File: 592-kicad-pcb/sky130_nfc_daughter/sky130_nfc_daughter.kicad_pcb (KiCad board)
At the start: 4 copper layers, 50 x 52 mm, 198 parts, among them J1 U.FL-R-SMT-1_80_, J10 U.FL-R-SMT-1_80_, J2 U.FL-R-SMT-1_80_, J3 U.FL-R-SMT-1_80_, J4 U.FL-R-SMT-1_80_, J5 U.FL-R-SMT-1_80_, J6 U.FL-R-SMT-1_80_, J7 U.FL-R-SMT-1_80_, J8 DF40C-40DS-0.4V_51_, J9 DF40C-40DS-0.4V_51_, SW1 SW_Push, U1 Caravel_QFN, U3 W25Q32JVZP

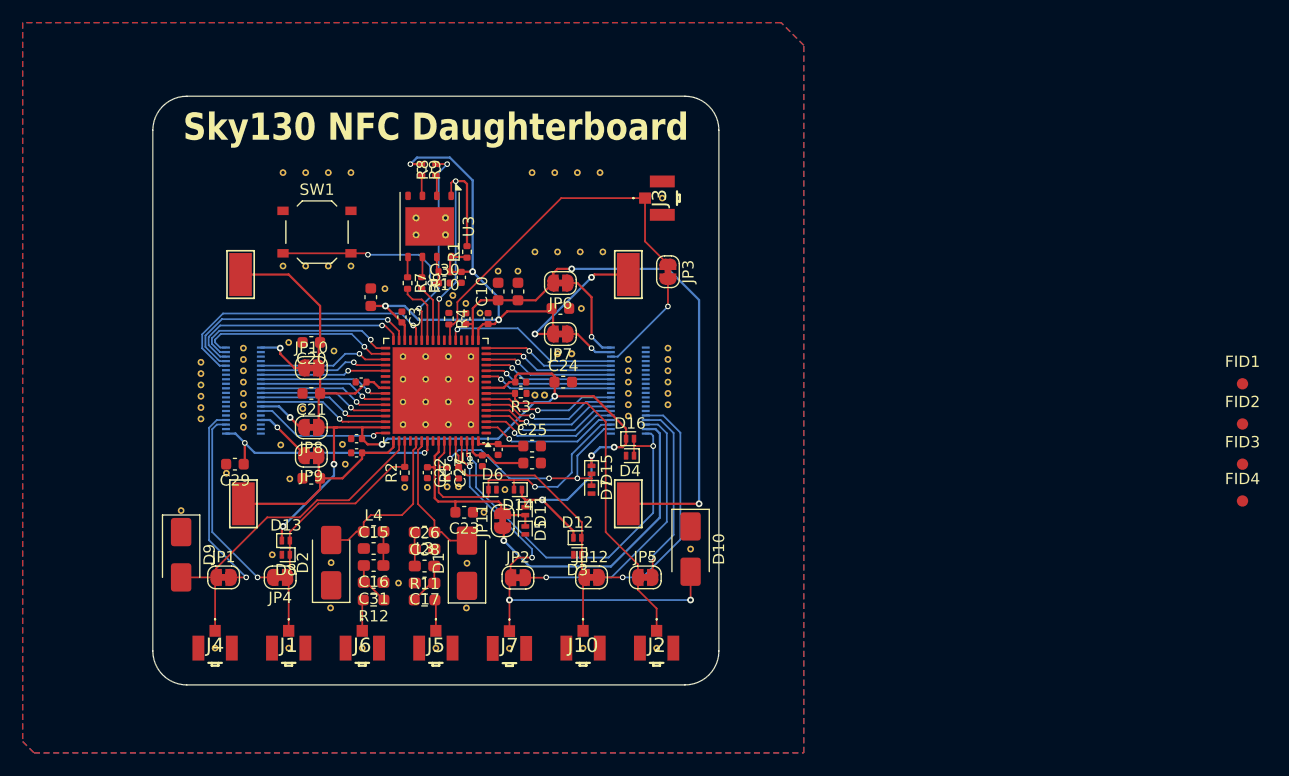
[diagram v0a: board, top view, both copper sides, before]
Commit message: finish daughter routing + silk
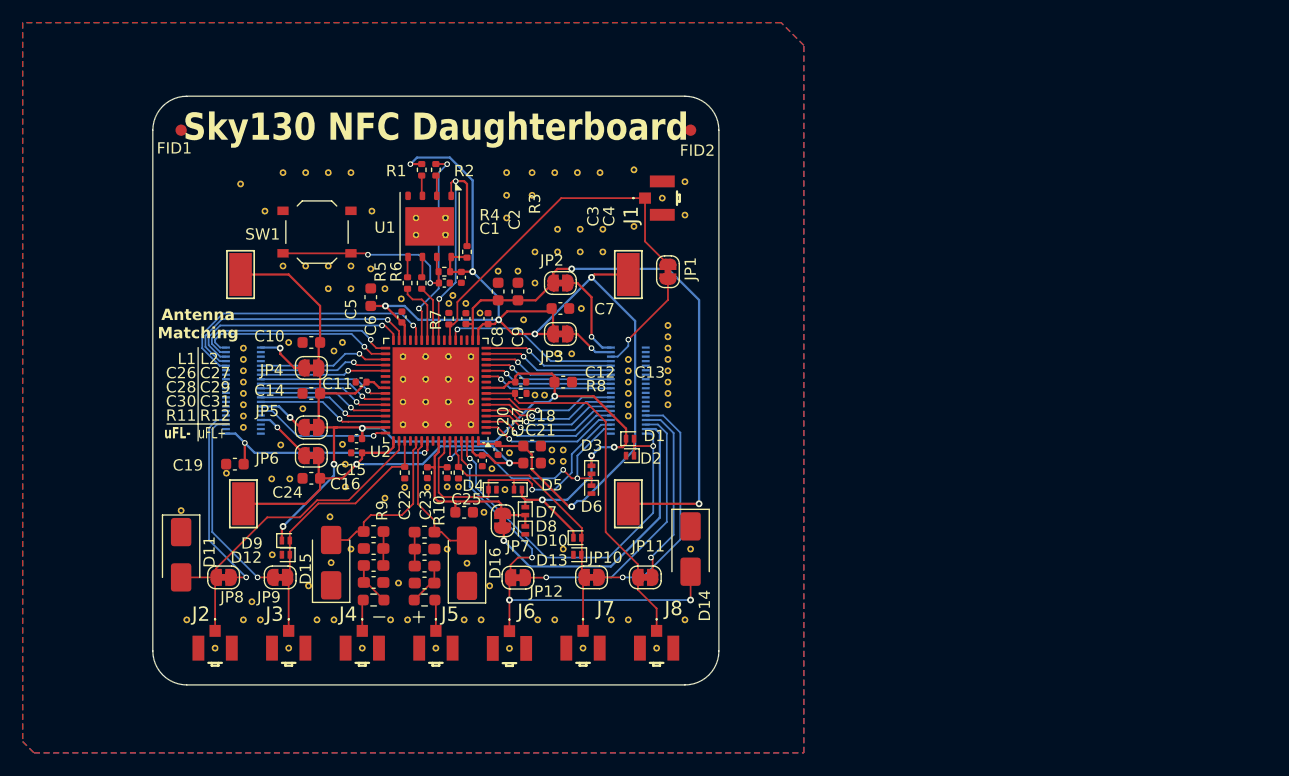
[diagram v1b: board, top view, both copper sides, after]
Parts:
- removed the ? at (53.8, 43.5)
- removed the ? at (53.8, 45.5)
- removed the ? at (53.8, 46.5)
- removed the ? at (53.8, 47.5)
- removed the ? at (53.8, 48.5)
- removed the ? at (53.8, 44.5)
- removed FID3, FID4: Fiducial, Fiducial:Fiducial_1mm_Mask2mm
- added ?: STITCHING_VIA_0p3mm, 592-partslib:STITCHING_VIA_0p3mm, F.Cu at (57.5, 66.2)
- added ?: STITCHING_VIA_0p3mm, 592-partslib:STITCHING_VIA_0p3mm, F.Cu at (70.5, 66.2)
- added ?: STITCHING_VIA_0p3mm, 592-partslib:STITCHING_VIA_0p3mm, F.Cu at (92.0, 31.5)
- added ?: STITCHING_VIA_0p3mm, 592-partslib:STITCHING_VIA_0p3mm, F.Cu at (78.5, 66.2)
- added ?: STITCHING_VIA_0p3mm, 592-partslib:STITCHING_VIA_0p3mm, F.Cu at (96.5, 30.5)
- added ?: STITCHING_VIA_0p3mm, 592-partslib:STITCHING_VIA_0p3mm, F.Cu at (85.8, 51.2)
- added ?: STITCHING_VIA_0p3mm, 592-partslib:STITCHING_VIA_0p3mm, F.Cu at (92.0, 26.5)
- added ?: STITCHING_VIA_0p3mm, 592-partslib:STITCHING_VIA_0p3mm, F.Cu at (85.0, 66.2)
- added ?: STITCHING_VIA_0p3mm, 592-partslib:STITCHING_VIA_0p3mm, F.Cu at (83.5, 66.2)
- added ?: STITCHING_VIA_0p3mm, 592-partslib:STITCHING_VIA_0p3mm, F.Cu at (52.5, 66.2)
- added ?: STITCHING_VIA_0p3mm, 592-partslib:STITCHING_VIA_0p3mm, F.Cu at (87.2, 31.8)
- added ?: STITCHING_VIA_0p3mm, 592-partslib:STITCHING_VIA_0p3mm, F.Cu at (96.5, 27.6)
- added ?: STITCHING_VIA_0p3mm, 592-partslib:STITCHING_VIA_0p3mm, F.Cu at (95.0, 41.2)
- added ?: STITCHING_VIA_0p3mm, 592-partslib:STITCHING_VIA_0p3mm, F.Cu at (59.4, 30.1)
- added ?: STITCHING_VIA_0p3mm, 592-partslib:STITCHING_VIA_0p3mm, F.Cu at (57.2, 27.8)
- added ?: STITCHING_VIA_0p3mm, 592-partslib:STITCHING_VIA_0p3mm, F.Cu at (58.2, 64.7)
- added ?: STITCHING_VIA_0p3mm, 592-partslib:STITCHING_VIA_0p3mm, F.Cu at (65.2, 57.1)
- added ?: STITCHING_VIA_0p3mm, 592-partslib:STITCHING_VIA_0p3mm, F.Cu at (96.5, 66.2)
- added ?: STITCHING_VIA_0p3mm, 592-partslib:STITCHING_VIA_0p3mm, F.Cu at (84.8, 51.2)
- added ?: STITCHING_VIA_0p3mm, 592-partslib:STITCHING_VIA_0p3mm, F.Cu at (80.8, 26.8)
- added ?: STITCHING_VIA_0p3mm, 592-partslib:STITCHING_VIA_0p3mm, F.Cu at (84.8, 52.2)
- added ?: STITCHING_VIA_0p3mm, 592-partslib:STITCHING_VIA_0p3mm, F.Cu at (91.5, 66.2)
- added ?: STITCHING_VIA_0p3mm, 592-partslib:STITCHING_VIA_0p3mm, F.Cu at (79.5, 52.9)
- added ?: STITCHING_VIA_0p3mm, 592-partslib:STITCHING_VIA_0p3mm, F.Cu at (65.5, 66.2)
- added ?: STITCHING_VIA_0p3mm, 592-partslib:STITCHING_VIA_0p3mm, F.Cu at (77.0, 66.2)
- added ?: STITCHING_VIA_0p3mm, 592-partslib:STITCHING_VIA_0p3mm, F.Cu at (72.0, 66.2)
- added ?: STITCHING_VIA_0p3mm, 592-partslib:STITCHING_VIA_0p3mm, F.Cu at (67.0, 60.0)
- added ?: STITCHING_VIA_0p3mm, 592-partslib:STITCHING_VIA_0p3mm, F.Cu at (82.2, 39.8)
- added ?: STITCHING_VIA_0p3mm, 592-partslib:STITCHING_VIA_0p3mm, F.Cu at (81.0, 51.5)
- added ?: STITCHING_VIA_0p3mm, 592-partslib:STITCHING_VIA_0p3mm, F.Cu at (83.0, 28.8)
- added ?: STITCHING_VIA_0p3mm, 592-partslib:STITCHING_VIA_0p3mm, F.Cu at (70.0, 55.5)
- added ?: STITCHING_VIA_0p3mm, 592-partslib:STITCHING_VIA_0p3mm, F.Cu at (83.2, 36.5)
- added ?: STITCHING_VIA_0p3mm, 592-partslib:STITCHING_VIA_0p3mm, F.Cu at (95.0, 40.2)
- added ?: STITCHING_VIA_0p3mm, 592-partslib:STITCHING_VIA_0p3mm, F.Cu at (65.0, 37.0)
- added ?: STITCHING_VIA_0p3mm, 592-partslib:STITCHING_VIA_0p3mm, F.Cu at (67.0, 37.0)
- added ?: STITCHING_VIA_0p3mm, 592-partslib:STITCHING_VIA_0p3mm, F.Cu at (80.8, 30.8)
- added ?: STITCHING_VIA_0p3mm, 592-partslib:STITCHING_VIA_0p3mm, F.Cu at (85.8, 60.0)
- added ?: STITCHING_VIA_0p3mm, 592-partslib:STITCHING_VIA_0p3mm, F.Cu at (85.2, 31.8)
- added ?: STITCHING_VIA_0p3mm, 592-partslib:STITCHING_VIA_0p3mm, F.Cu at (68.8, 30.1)
- added ?: STITCHING_VIA_0p3mm, 592-partslib:STITCHING_VIA_0p3mm, F.Cu at (66.2, 41.8)
- added ?: STITCHING_VIA_0p3mm, 592-partslib:STITCHING_VIA_0p3mm, F.Cu at (66.5, 54.5)
- added ?: STITCHING_VIA_0p3mm, 592-partslib:STITCHING_VIA_0p3mm, F.Cu at (71.5, 37.9)
- added ?: STITCHING_VIA_0p3mm, 592-partslib:STITCHING_VIA_0p3mm, F.Cu at (64.0, 66.2)
- added ?: STITCHING_VIA_0p3mm, 592-partslib:STITCHING_VIA_0p3mm, F.Cu at (85.8, 52.2)
- added ?: STITCHING_VIA_0p3mm, 592-partslib:STITCHING_VIA_0p3mm, F.Cu at (90.0, 66.2)
- added ?: STITCHING_VIA_0p3mm, 592-partslib:STITCHING_VIA_0p3mm, F.Cu at (60.0, 53.8)
- added ?: STITCHING_VIA_0p3mm, 592-partslib:STITCHING_VIA_0p3mm, F.Cu at (75.5, 60.0)
- added ?: STITCHING_VIA_0p3mm, 592-partslib:STITCHING_VIA_0p3mm, F.Cu at (59.0, 66.2)
- added ?: STITCHING_VIA_0p3mm, 592-partslib:STITCHING_VIA_0p3mm, F.Cu at (89.2, 31.8)
- added ?: STITCHING_VIA_0p3mm, 592-partslib:STITCHING_VIA_0p3mm, F.Cu at (80.8, 28.8)
- added ?: STITCHING_VIA_0p3mm, 592-partslib:STITCHING_VIA_0p3mm, F.Cu at (68.8, 35.2)
- ? (x86): value (none) -> STITCHING_VIA_0p3mm; footprint (none) -> 592-partslib:STITCHING_VIA_0p3mm
- STITCHM1: value StitchingVia-0.3mm -> STITCHING_VIA_0p3mm; footprint flyingcarsfootprints:StitchingVia-0.3mm -> 592-partslib:STITCHING_VIA_0p3mm
- STITCHM2, STITCHM3, STITCHM4, STITCHM5: renamed from STITCHM1; value StitchingVia-0.3mm -> STITCHING_VIA_0p3mm; footprint flyingcarsfootprints:StitchingVia-0.3mm -> 592-partslib:STITCHING_VIA_0p3mm
- moved FID1 96.4 mm to (52.0, 23.0)
- moved FID2 55.2 mm to (97.0, 23.0)
- moved ? 2.83 mm to (79.2, 63.2)
- moved ? 2.76 mm to (63.2, 63.2)
- renumbered C30 to C1, C20 to C10, C12 to C11, C13 to C12, C24 to C13, C21 to C14, C11 to C15, C6 to C16, C8 to C17, C25 to C18, C29 to C19, C9 to C2, C5 to C20, C14 to C21, C27 to C23, C18 to C24, C23 to C25, C15 to C26, C26 to C27, C16 to C28, C28 to C29, C10 to C3, C31 to C30, C17 to C31, C2 to C4, C19 to C5, C3 to C6, C1 to C7, C4 to C8, C7 to C9, D16 to D1, D12 to D10, D9 to D11, D8 to D12, D3 to D13, D10 to D14, D2 to D15, D1 to D16, D4 to D2, D15 to D3, D6 to D4, D14 to D5, D7 to D6, D11 to D7, D5 to D8, D13 to D9, J3 to J1, J8 to J10, J4 to J2, J1 to J3, J6 to J4, J7 to J6, J10 to J7, J2 to J8, JP3 to JP1, JP12 to JP10, JP5 to JP11, JP2 to JP12, JP6 to JP2, JP7 to JP3, JP10 to JP4, JP8 to JP5, JP9 to JP6, JP11 to JP7, JP1 to JP8, JP4 to JP9, L4 to L1, L3 to L2, R9 to R1, R5 to R10, R12 to R11, R11 to R12, R8 to R2, R1 to R3, R10 to R4, R7 to R5, R4 to R7, R3 to R8, R2 to R9, TP4 to TP1, TP1 to TP4, U3 to U1, U1 to U2
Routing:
- net vddio_vdda_mgmt_3v3: track 68.3 -> 103.8 mm, vias 6 -> 7
- net vccd_user_1v8: track 24.7 -> 39.4 mm, vias 0 -> 2
- net vdda_user_3v3: track 100.2 -> 101.3 mm
- net /RESET_EXT: track 22.4 -> 23.0 mm
- net /VREF_EXT: track 27.0 -> 27.5 mm
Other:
- board text added: "Antenna Matching"
- board text added: "uFL+"
- board text added: "uFL-"

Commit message: add qfn small epad footprint, update silk on daughterboard, add fiducials, adjust mezzanine spacing
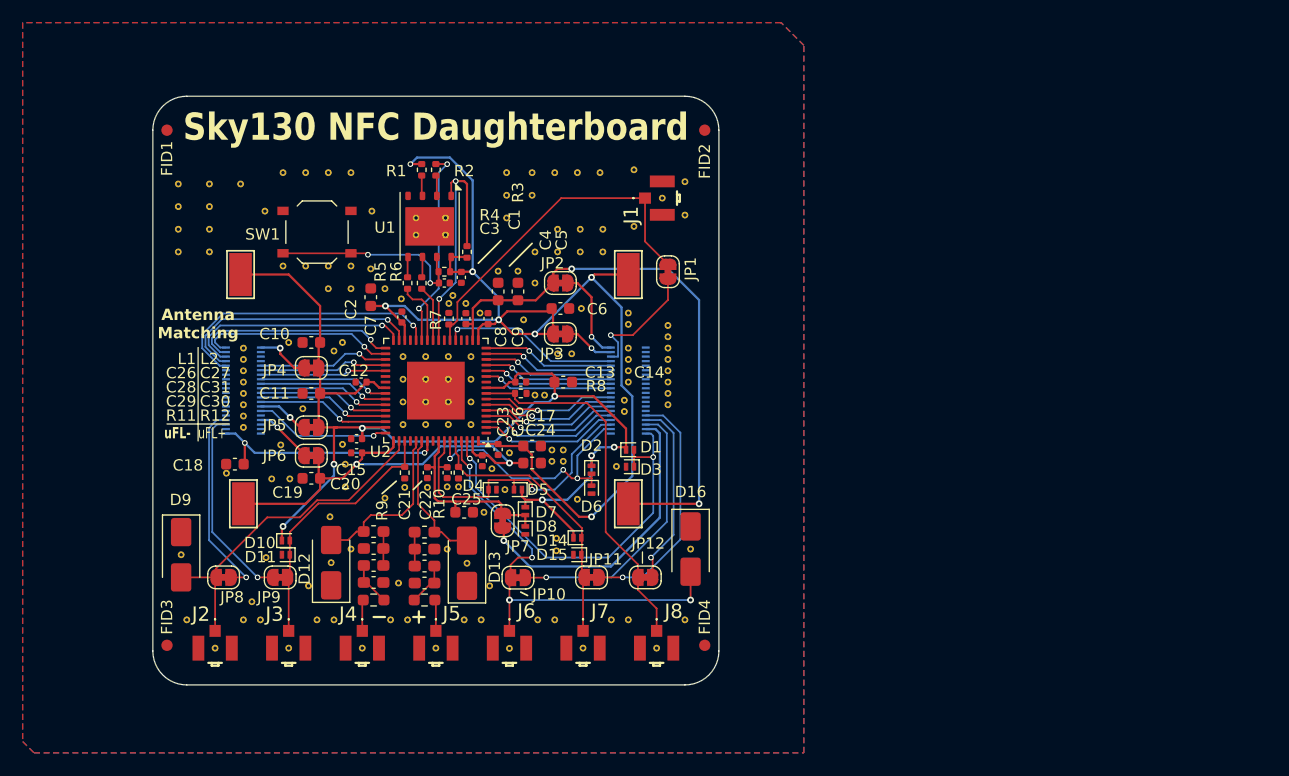
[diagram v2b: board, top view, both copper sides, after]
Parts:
- removed the ? at (91.5, 47.2)
- added ?: STITCHING_VIA_0p3mm, 592-partslib:STITCHING_VIA_0p3mm, F.Cu at (91.2, 46.9)
- added ?: STITCHING_VIA_0p3mm, 592-partslib:STITCHING_VIA_0p3mm, F.Cu at (85.2, 59.0)
- added ?: STITCHING_VIA_0p3mm, 592-partslib:STITCHING_VIA_0p3mm, F.Cu at (91.5, 42.2)
- added ?: STITCHING_VIA_0p3mm, 592-partslib:STITCHING_VIA_0p3mm, F.Cu at (54.5, 31.8)
- added ?: STITCHING_VIA_0p3mm, 592-partslib:STITCHING_VIA_0p3mm, F.Cu at (51.8, 31.8)
- added ?: STITCHING_VIA_0p3mm, 592-partslib:STITCHING_VIA_0p3mm, F.Cu at (90.5, 52.7)
- added ?: STITCHING_VIA_0p3mm, 592-partslib:STITCHING_VIA_0p3mm, F.Cu at (51.8, 33.8)
- added ?: STITCHING_VIA_0p3mm, 592-partslib:STITCHING_VIA_0p3mm, F.Cu at (51.8, 29.8)
- added ?: STITCHING_VIA_0p3mm, 592-partslib:STITCHING_VIA_0p3mm, F.Cu at (54.5, 27.8)
- added ?: STITCHING_VIA_0p3mm, 592-partslib:STITCHING_VIA_0p3mm, F.Cu at (91.5, 39.1)
- added ?: STITCHING_VIA_0p3mm, 592-partslib:STITCHING_VIA_0p3mm, F.Cu at (54.5, 29.8)
- added ?: STITCHING_VIA_0p3mm, 592-partslib:STITCHING_VIA_0p3mm, F.Cu at (51.8, 27.8)
- added ?: STITCHING_VIA_0p3mm, 592-partslib:STITCHING_VIA_0p3mm, F.Cu at (54.5, 33.8)
- added ?: STITCHING_VIA_0p3mm, 592-partslib:STITCHING_VIA_0p3mm, F.Cu at (87.0, 55.6)
- added FID3: Fiducial, Fiducial:Fiducial_1mm_Mask2mm, F.Cu at (50.8, 68.5)
- added FID4: Fiducial, Fiducial:Fiducial_1mm_Mask2mm, F.Cu at (98.2, 68.5)
- U2: footprint Package_DFN_QFN:QFN-64-1EP_9x9mm_P0.5mm_EP7.65x7.65mm -> 592-partslib:QFN-64-1EP_9x9mm_P0.5mm_EP7.65x7.65mm_SMALL_EPAD
- moved ? 8.10 mm to (91.5, 40.1)
- moved ? 3.90 mm to (52.0, 60.5)
- moved ? 1.64 mm to (91.2, 47.9)
- moved FID1 1.25 mm to (50.8, 23.0)
- moved FID2 1.25 mm to (98.2, 23.0)
- moved D1 0.98 mm to (91.7, 51.2)
- moved D3 0.98 mm to (91.7, 52.7)
- moved ? 0.62 mm to (85.2, 60.1)
- moved ? 0.60 mm to (59.5, 60.8)
- renumbered C2 to C1, C14 to C11, C11 to C12, C12 to C13, C13 to C14, C17 to C16, C18 to C17, C19 to C18, C24 to C19, C5 to C2, C16 to C20, C22 to C21, C23 to C22, C20 to C23, C21 to C24, C30 to C29, C1 to C3, C31 to C30, C29 to C31, C3 to C4, C4 to C5, C7 to C6, C6 to C7, D9 to D10, D12 to D11, D15 to D12, D16 to D13, D10 to D14, D13 to D15, D14 to D16, D3 to D2, D2 to D3, D11 to D9, JP12 to JP10, JP10 to JP11, JP11 to JP12
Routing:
- net vddio_vdda_mgmt_3v3: track 103.8 -> 105.6 mm
- net /J_clk: track 9.29 -> 11.0 mm

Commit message: add MH for orientation indicator
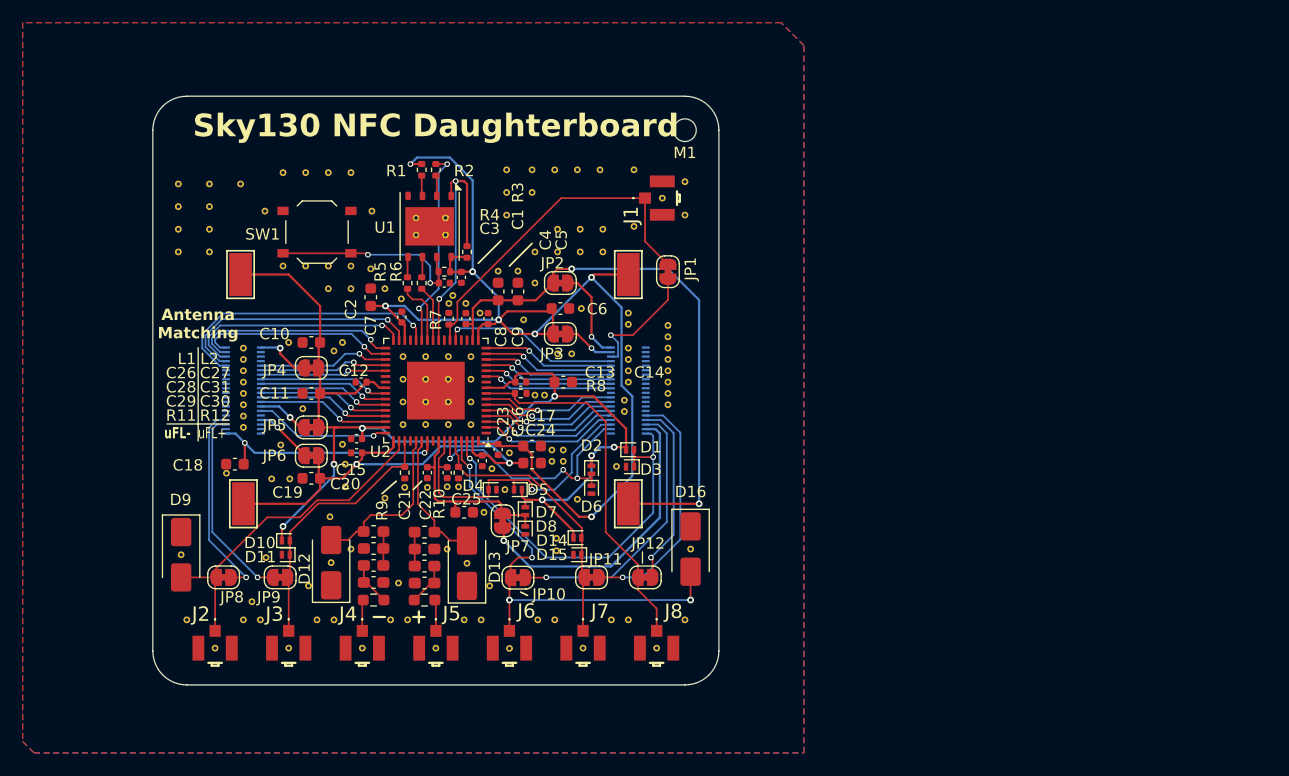
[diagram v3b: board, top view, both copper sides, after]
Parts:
- removed FID1, FID2, FID3, FID4: Fiducial, Fiducial:Fiducial_1mm_Mask2mm
- added M1: MountingHole_2mm, MountingHole:MountingHole_2mm, F.Cu at (96.5, 23.0)
- moved ? 0.25 mm to (87.0, 26.5)
- moved ? 0.25 mm to (80.8, 28.5)
- moved ? 0.25 mm to (89.0, 26.5)
- moved ? 0.25 mm to (85.0, 26.5)
- moved ? 0.25 mm to (80.8, 26.5)
- moved ? 0.25 mm to (83.0, 28.5)
- moved ? 0.25 mm to (80.8, 30.5)
- moved ? 0.25 mm to (83.0, 26.5)
